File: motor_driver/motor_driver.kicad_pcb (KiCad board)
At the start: 2 copper layers, 39 x 25 mm, 23 parts

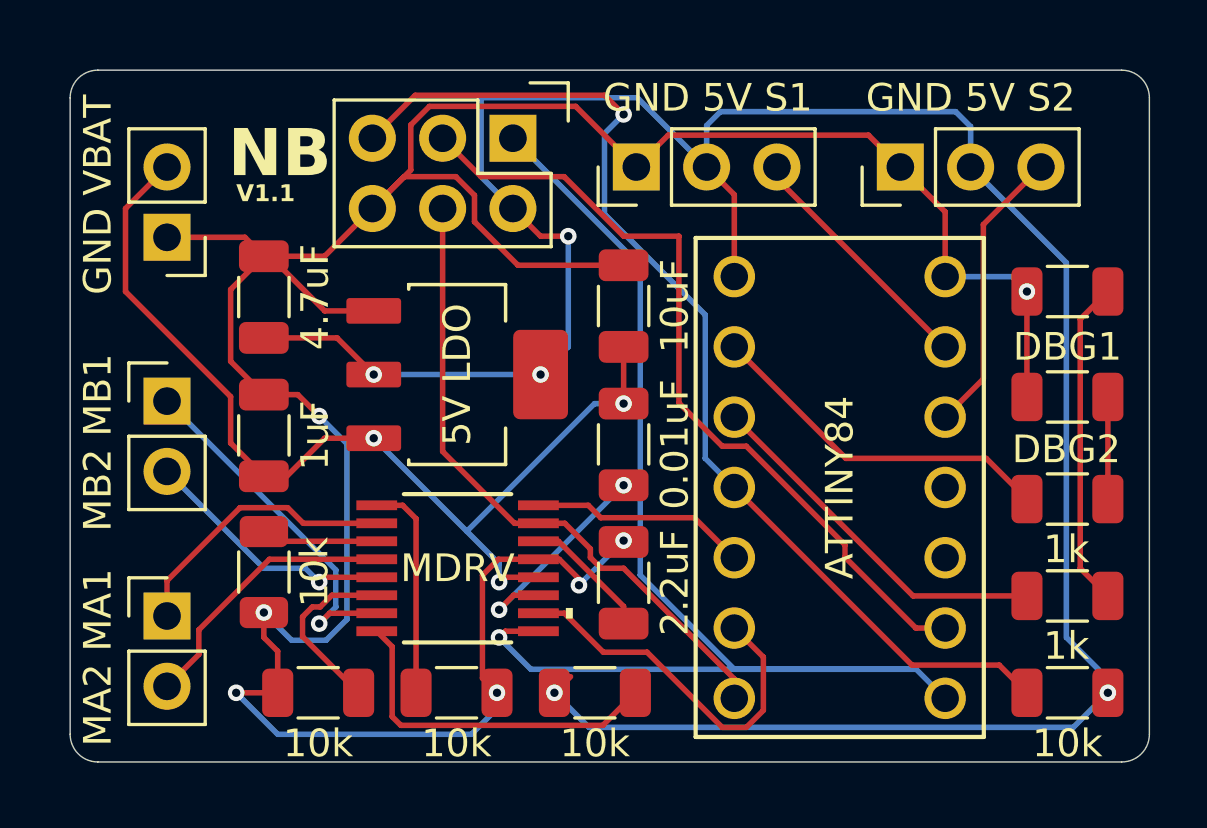
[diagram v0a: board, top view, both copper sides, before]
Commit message: updated pcb schematic with changes from testing
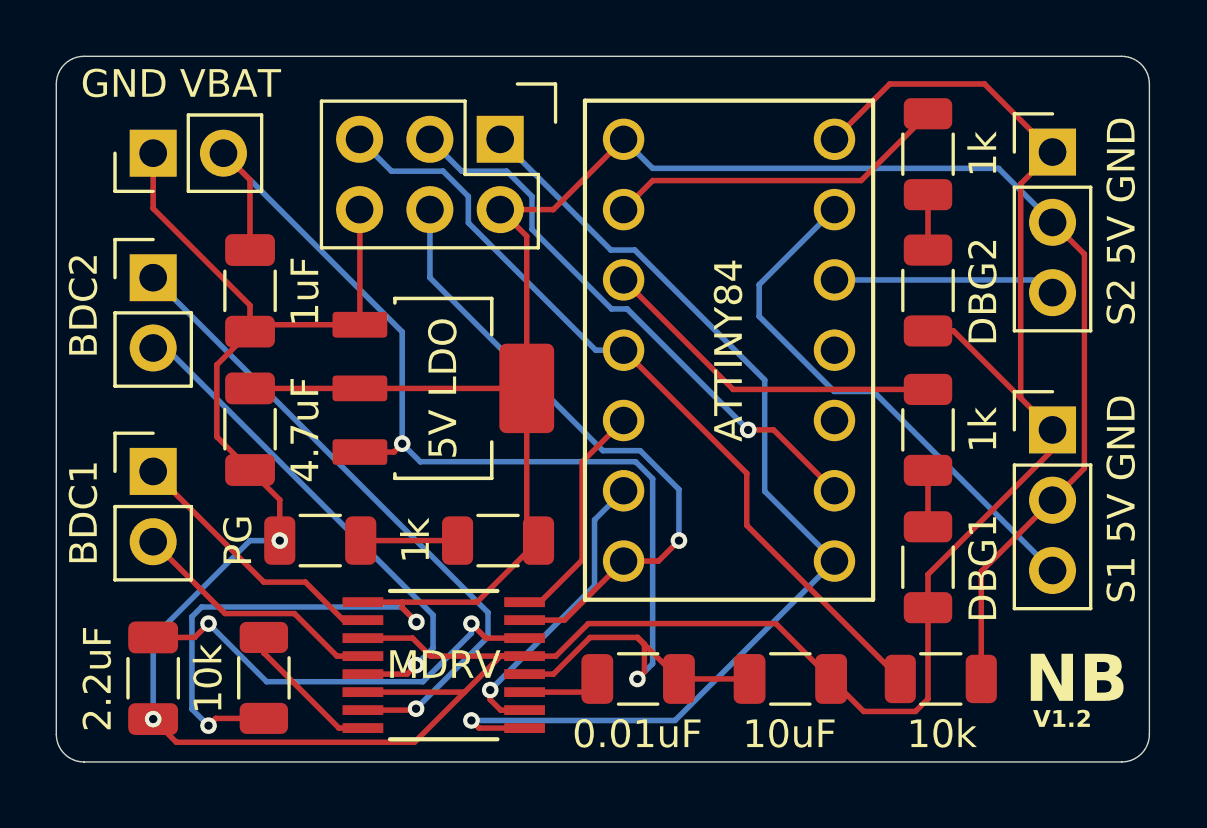
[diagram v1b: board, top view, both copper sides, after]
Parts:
- removed the 10k at (142.0, 68.0)
- removed the 10k at (137.0, 68.0)
- removed the 10k at (132.0, 68.0)
- removed the 10k at (130.0, 63.6)
- removed the 10k at (159.0, 68.0)
- removed the 1k at (159.0, 64.5)
- removed the 1k at (159.0, 61.0)
- removed the 5V LDO at (137.0, 56.5)
- removed GND 5V S1: Conn_01x03_Pin, Connector_PinHeader_2.54mm:PinHeader_1x03_P2.54mm_Vertical
- removed GND 5V S2: Conn_01x03_Pin, Connector_PinHeader_2.54mm:PinHeader_1x03_P2.54mm_Vertical
- removed MA2 MA1: Conn_01x02_Pin, Connector_PinHeader_2.54mm:PinHeader_1x02_P2.54mm_Vertical
- removed MB2 MB1: Conn_01x02_Pin, Connector_PinHeader_2.54mm:PinHeader_1x02_P2.54mm_Vertical
- removed the MDRV at (137.0, 63.5)
- added 10k: 10k, Resistor_SMD:R_1206_3216Metric, F.Cu at (154.5, 67.5)
- added 10k: 10k, Resistor_SMD:R_1206_3216Metric, F.Cu at (130.0, 67.5)
- added 1k: 1k, Resistor_SMD:R_1206_3216Metric, F.Cu at (154.0, 58.5)
- added 1k: 1k, Resistor_SMD:R_1206_3216Metric, F.Cu at (138.5, 62.5)
- added 1k: 1k, Resistor_SMD:R_1206_3216Metric, F.Cu at (154.0, 48.5)
- added 5V LDO: LDL1117S50R_, footprints:SOT230P700X180-4N, F.Cu at (136.5, 57.0)
- added BDC1: Conn_01x02_Pin, Connector_PinHeader_2.54mm:PinHeader_1x02_P2.54mm_Vertical, F.Cu at (126.0, 60.0)
- added BDC2: Conn_01x02_Pin, Connector_PinHeader_2.54mm:PinHeader_1x02_P2.54mm_Vertical, F.Cu at (126.0, 53.0)
- added MDRV: DRV8833PWR, footprints:DRV8833PWR, F.Cu at (136.5, 67.0)
- added PG: LED, Resistor_SMD:R_1206_3216Metric, F.Cu at (132.0, 62.5)
- added S1 5V GND: Conn_01x03_Pin, Connector_PinHeader_2.54mm:PinHeader_1x03_P2.54mm_Vertical, F.Cu at (158.5, 58.5)
- added S2 5V GND: Conn_01x03_Pin, Connector_PinHeader_2.54mm:PinHeader_1x03_P2.54mm_Vertical, F.Cu at (158.5, 48.5)
- ATTINY84: footprint A14_LC_TT:A14-LC-TT_ASM -> footprints:A14-LC-TT_ASM
- moved 2.2uF 17.3 mm to (126.0, 67.5), turned to 90 degrees
- moved 10uF 14.8 mm to (149.0, 67.5), turned to 180 degrees
- moved DBG1 11.2 mm to (154.0, 63.5), turned to 90 degrees
- moved 0.01uF 8.49 mm to (143.5, 67.5), turned to 180 degrees
- moved ATTINY84 6.37 mm to (150.6, 48.0)
- moved DBG2 6.34 mm to (154.0, 53.5), turned to 90 degrees
- moved 1uF 5.25 mm to (129.5, 53.5), turned to 90 degrees
- moved 4.7uF 4.80 mm to (129.5, 58.5), turned to 90 degrees
- moved GND VBAT 3.08 mm to (126.0, 48.5), turned to 90 degrees
- moved FLASH1 0.46 mm to (138.5, 48.0)
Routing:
- net Net-(U2-VINT): track 4.68 -> 15.8 mm, vias 0 -> 2
- net Net-(BDC2-Pin_1): track 13.1 -> 23.6 mm
- net Net-(PWM_In1-Pin_3): track 9.02 -> 19.4 mm
- net VBAT: track 36.6 -> 46.8 mm, vias 3 -> 2
- net RESET: track 39.4 -> 29.3 mm, vias 1 -> 0
- net Net-(DBG1-A): track 11.8 -> 2.04 mm
- net MISO: track 47.6 -> 38.3 mm
- net Net-(BDC2-Pin_2): track 9.31 -> 18.2 mm
- net SCK: track 29.3 -> 20.6 mm, vias 0 -> 1
- net Net-(U2-NSLEEP): track 7.91 -> 0.00 mm
- net Net-(U2-NFAULT): track 12.7 -> 5.27 mm
- net Net-(U2-BISEN): track 6.59 -> 0.00 mm
- net GND: track 106.2 -> 112.2 mm, vias 7 -> 2
- net 5V: track 92.3 -> 86.3 mm, vias 5 -> 2
- net Net-(U2-VCP): track 8.00 -> 2.83 mm, vias 2 -> 0
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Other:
- board size 39 x 25 mm -> 39.5 x 25.5 mm
- board text added: "V1.2"
- board text removed: "V1.1"
